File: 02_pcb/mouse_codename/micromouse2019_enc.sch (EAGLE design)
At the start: 0 parts

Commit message: schematic and pcb created
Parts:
- added C1: (no value), rcl:C-USC0402
- added IC1: AS5047D-ATSM, parts_not_managed:AS5047D-ATSM
- added R1, R2, R3: (no value), rcl:R-US_R0402
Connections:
- new net +3V3: C1.1, IC1.VDD, IC1.VDD3V, R1.2
- new net A: IC1.B
- new net B: IC1.A
- new net GND: C1.2, IC1.GND, IC1.TEST, R2.1, R3.1
- new net I: IC1.I/PWM
- new net N$1: IC1.CSN, R1.1
- new net N$2: IC1.CLK, R2.2
- new net N$3: IC1.MOSI, R3.2
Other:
- note added: "The LDO regulator is not intended to power any other loads, and it needs a 1 μF capacitor to ground located close to the chip"
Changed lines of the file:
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@@
 </classes>
 <parts>
+<part name="IC1" library="parts_not_managed" deviceset="AS5047D-ATSM" device=""/>
+<part name="R1" library="rcl" library_urn="urn:adsk.eagle:library:334" deviceset="R-US_" device="R0402" package3d_urn="urn:adsk.eagle:package:23547/3"/>
+<part name="R2" library="rcl" library_urn="urn:adsk.eagle:library:334" deviceset="R-US_" device="R0402" package3d_urn="urn:adsk.eagle:package:23547/3"/>
+<part name="R3" library="rcl" library_urn="urn:adsk.eagle:library:334" deviceset="R-US_" device="R0402" package3d_urn="urn:adsk.eagle:package:23547/3"/>
+<part name="+3V1" library="supply1" library_urn="urn:adsk.eagle:library:371" deviceset="+3V3" device=""/>
+<part name="GND1" library="supply1" library_urn="urn:adsk.eagle:library:371" deviceset="GND" device=""/>
+<part name="GND2" library="supply1" library_urn="urn:adsk.eagle:library:371" deviceset="GND" device=""/>
+<part name="GND3" library="supply1" library_urn="urn:adsk.eagle:library:371" deviceset="GND" device=""/>
+<part name="GND4" library="supply1" library_urn="urn:adsk.eagle:library:371" deviceset="GND" device=""/>
+<part name="C1" library="rcl" library_urn="urn:adsk.eagle:library:334" deviceset="C-US" device="C0402" package3d_urn="urn:adsk.eagle:package:23626/2"/>
+<part name="GND5" library="supply1" library_urn="urn:adsk.eagle:library:371" deviceset="GND" device=""/>
+<part name="+3V2" library="supply1" library_urn="urn:adsk.eagle:library:371" deviceset="+3V3" device=""/>
+<part name="GND6" library="supply1" library_urn="urn:adsk.eagle:library:371" deviceset="GND" device=""/>
+<part name="+3V3" library="supply1" library_urn="urn:adsk.eagle:library:371" deviceset="+3V3" device=""/>
 </parts>
 <sheets>
 <sheet>
 <plain>
+<text x="139.7" y="15.24" size="1.778" layer="97"> The LDO regulator is not intended to power any other
+loads, and it needs a 1 μF capacitor to ground located close to
+the chip</text>
 </plain>
 <instances>
+<instance part="IC1" gate="G$1" x="45.72" y="66.04" smashed="yes">
+<attribute name="NAME" x="72.39" y="73.66" size="1.778" layer="95" align="center-left"/>
+<attribute name="VALUE" x="72.39" y="71.12" size="1.778" layer="96" align="center-left"/>
+</instance>
+<instance part="R1" gate="G$1" x="40.64" y="73.66" smashed="yes" rot="R90">
+<attribute name="NAME" x="39.1414" y="69.85" size="1.778" layer="95" rot="R90"/>
+<attribute name="VALUE" x="43.942" y="69.85" size="1.778" layer="96" rot="R90"/>
+</instance>
+<instance part="R2" gate="G$1" x="17.78" y="50.8" smashed="yes" rot="R90">
+<attribute name="NAME" x="16.2814" y="46.99" size="1.778" layer="95" rot="R90"/>
+<attribute name="VALUE" x="21.082" y="46.99" size="1.778" layer="96" rot="R90"/>
+</instance>
+<instance part="R3" gate="G$1" x="25.4" y="50.8" smashed="yes" rot="R90">
+<attribute name="NAME" x="23.9014" y="46.99" size="1.778" layer="95" rot="R90"/>
+<attribute name="VALUE" x="28.702" y="46.99" size="1.778" layer="96" rot="R90"/>
+</instance>
+<instance part="+3V1" gate="G$1" x="40.64" y="86.36" smashed="yes">
+<attribute name="VALUE" x="38.862" y="81.788" size="1.778" layer="96" rot="R90"/>
+</instance>
+<instance part="GND1" gate="1" x="17.78" y="40.64" smashed="yes">
+<attribute name="VALUE" x="15.24" y="38.1" size="1.778" layer="96"/>
+</instance>
+<instance part="GND2" gate="1" x="25.4" y="40.64" smashed="yes">
+<attribute name="VALUE" x="22.86" y="38.1" size="1.778" layer="96"/>
+</instance>
+<instance part="GND3" gate="1" x="106.68" y="40.64" smashed="yes">
+<attribute name="VALUE" x="104.14" y="38.1" size="1.778" layer="96"/>
+</instance>
+<instance part="GND4" gate="1" x="33.02" y="40.64" smashed="yes">
+<attribute name="VALUE" x="30.48" y="38.1" size="1.778" layer="96"/>
+</instance>
+<instance part="C1" gate="G$1" x="88.9" y="50.8" smashed="yes">
+<attribute name="NAME" x="89.916" y="51.435" size="1.778" layer="95"/>
+<attribute name="VALUE" x="89.916" y="46.609" size="1.778" layer="96"/>
+</instance>
+<instance part="GND5" gate="1" x="88.9" y="40.64" smashed="yes">
+<attribute name="VALUE" x="86.36" y="38.1" size="1.778" layer="96"/>
+</instance>
+<instance part="+3V2" gate="G$1" x="99.06" y="60.96" smashed="yes">
+<attribute name="VALUE" x="97.536" y="55.88" size="1.778" layer="96" rot="R90"/>
+</instance>
+<instance part="GND6" gate="1" x="129.54" y="40.64" smashed="yes">
+<attribute name="VALUE" x="127" y="38.1" size="1.778" layer="96"/>
+</instance>
+<instance part="+3V3" gate="G$1" x="129.54" y="71.12" smashed="yes">
+<attribute name="VALUE" x="128.016" y="66.04" size="1.778" layer="96" rot="R90"/>
+</instance>
 </instances>
 <busses>
 </busses>
 <nets>
+<net name="N$1" class="0">
+<segment>
+<pinref part="IC1" gate="G$1" pin="CSN"/>
+<pinref part="R1" gate="G$1" pin="1"/>
+<wire x1="45.72" y1="66.04" x2="40.64" y2="66.04" width="0.1524" layer="91"/>
+<wire x1="40.64" y1="66.04" x2="40.64" y2="68.58" width="0.1524" layer="91"/>
+</segment>
+</net>
+<net name="+3V3" class="0">
+<segment>
+<pinref part="R1" gate="G$1" pin="2"/>
+<pinref part="+3V1" gate="G$1" pin="+3V3"/>
+<wire x1="40.64" y1="78.74" x2="40.64" y2="83.82" width="0.1524" layer="91"/>
+</segment>
+<segment>
+<wire x1="99.06" y1="58.42" x2="99.06" y2="55.88" width="0.1524" layer="91"/>
+<pinref part="IC1" gate="G$1" pin="VDD3V"/>
+<wire x1="76.2" y1="60.96" x2="78.74" y2="60.96" width="0.1524" layer="91"/>
+<wire x1="78.74" y1="60.96" x2="78.74" y2="58.42" width="0.1524" layer="91"/>
+<pinref part="IC1" gate="G$1" pin="VDD"/>
+<wire x1="76.2" y1="58.42" x2="78.74" y2="58.42" width="0.1524" layer="91"/>
+<pinref part="C1" gate="G$1" pin="1"/>
+<wire x1="88.9" y1="53.34" x2="88.9" y2="55.88" width="0.1524" layer="91"/>
+<wire x1="88.9" y1="55.88" x2="88.9" y2="58.42" width="0.1524" layer="91"/>
+<wire x1="88.9" y1="58.42" x2="78.74" y2="58.42" width="0.1524" layer="91"/>
+<junction x="78.74" y="58.42"/>
+<wire x1="99.06" y1="55.88" x2="88.9" y2="55.88" width="0.1524" layer="91"/>
+<junction x="88.9" y="55.88"/>
+<pinref part="+3V2" gate="G$1" pin="+3V3"/>
+</segment>
+<segment>
+<pinref part="+3V3" gate="G$1" pin="+3V3"/>
+<wire x1="134.62" y1="60.96" x2="129.54" y2="60.96" width="0.1524" layer="91"/>
+<wire x1="129.54" y1="60.96" x2="129.54" y2="68.58" width="0.1524" layer="91"/>
+</segment>
+</net>
+<net name="N$2" class="0">
+<segment>
+<pinref part="IC1" gate="G$1" pin="CLK"/>
+<pinref part="R2" gate="G$1" pin="2"/>
+<wire x1="45.72" y1="63.5" x2="17.78" y2="63.5" width="0.1524" layer="91"/>
+<wire x1="17.78" y1="63.5" x2="17.78" y2="55.88" width="0.1524" layer="91"/>
+</segment>
+</net>
+<net name="N$3" class="0">
+<segment>
+<pinref part="IC1" gate="G$1" pin="MOSI"/>
+<pinref part="R3" gate="G$1" pin="2"/>
+<wire x1="45.72" y1="58.42" x2="25.4" y2="58.42" width="0.1524" layer="91"/>
+<wire x1="25.4" y1="58.42" x2="25.4" y2="55.88" width="0.1524" layer="91"/>
+</segment>
+</net>
+<net name="GND" class="0">
+<segment>
+<pinref part="R2" gate="G$1" pin="1"/>
+<pinref part="GND1" gate="1" pin="GND"/>
+<wire x1="17.78" y1="45.72" x2="17.78" y2="43.18" width="0.1524" layer="91"/>
+</segment>
+<segment>
+<pinref part="R3" gate="G$1" pin="1"/>
+<pinref part="GND2" gate="1" pin="GND"/>
+<wire x1="25.4" y1="45.72" x2="25.4" y2="43.18" width="0.1524" layer="91"/>
+</segment>
+<segment>
+<pinref part="IC1" gate="G$1" pin="GND"/>
+<wire x1="76.2" y1="63.5" x2="106.68" y2="63.5" width="0.1524" layer="91"/>
+<pinref part="GND3" gate="1" pin="GND"/>
+<wire x1="106.68" y1="63.5" x2="106.68" y2="43.18" width="0.1524" layer="91"/>
+</segment>
+<segment>
+<pinref part="IC1" gate="G$1" pin="TEST"/>
+<pinref part="GND4" gate="1" pin="GND"/>
+<wire x1="45.72" y1="55.88" x2="33.02" y2="55.88" width="0.1524" layer="91"/>
+<wire x1="33.02" y1="55.88" x2="33.02" y2="43.18" width="0.1524" layer="91"/>
+</segment>
+<segment>
+<pinref part="C1" gate="G$1" pin="2"/>
+<pinref part="GND5" gate="1" pin="GND"/>
+<wire x1="88.9" y1="45.72" x2="88.9" y2="43.18" width="0.1524" layer="91"/>
+</segment>
+<segment>
+<wire x1="134.62" y1="50.8" x2="129.54" y2="50.8" width="0.1524" layer="91"/>
+<pinref part="GND6" gate="1" pin="GND"/>
+<wire x1="129.54" y1="50.8" x2="129.54" y2="43.18" width="0.1524" layer="91"/>
+</segment>
+</net>
+<net name="A" class="0">
+<segment>
+<pinref part="IC1" gate="G$1" pin="B"/>
+<wire x1="45.72" y1="53.34" x2="40.64" y2="53.34" width="0.1524" layer="91"/>
+<label x="40.64" y="53.34" size="1.778" layer="95"/>
+</segment>
+<segment>
+<wire x1="134.62" y1="58.42" x2="124.46" y2="58.42" width="0.1524" layer="91"/>
+<label x="124.46" y="58.42" size="1.778" layer="95"/>
+</segment>
+</net>
+<net name="B" class="0">
+<segment>
+<pinref part="IC1" gate="G$1" pin="A"/>
+<wire x1="45.72" y1="50.8" x2="40.64" y2="50.8" width="0.1524" layer="91"/>
+<label x="40.64" y="50.8" size="1.778" layer="95"/>
+</segment>
+<segment>
+<wire x1="134.62" y1="55.88" x2="124.46" y2="55.88" width="0.1524" layer="91"/>
+<label x="124.46" y="55.88" size="1.778" layer="95"/>
+</segment>
+</net>
+<net name="I" class="0">
+<segment>
+<pinref part="IC1" gate="G$1" pin="I/PWM"/>
+<wire x1="76.2" y1="66.04" x2="81.28" y2="66.04" width="0.1524" layer="91"/>
+<label x="78.74" y="66.04" size="1.778" layer="95"/>
+</segment>
+<segment>
+<wire x1="134.62" y1="53.34" x2="124.46" y2="53.34" width="0.1524" layer="91"/>
+<label x="124.46" y="53.34" size="1.778" layer="95"/>
+</segment>
+</net>
 </nets>
 </sheet>
@@
 </drawing>
 <compatibility>
+<note version="6.3" minversion="6.2.2" severity="warning">
+Since Version 6.2.2 text objects can contain more than one line,
+which will not be processed correctly with this version.
+</note>
 <note version="8.2" severity="warning">
 Since Version 8.2, EAGLE supports online libraries. The ids

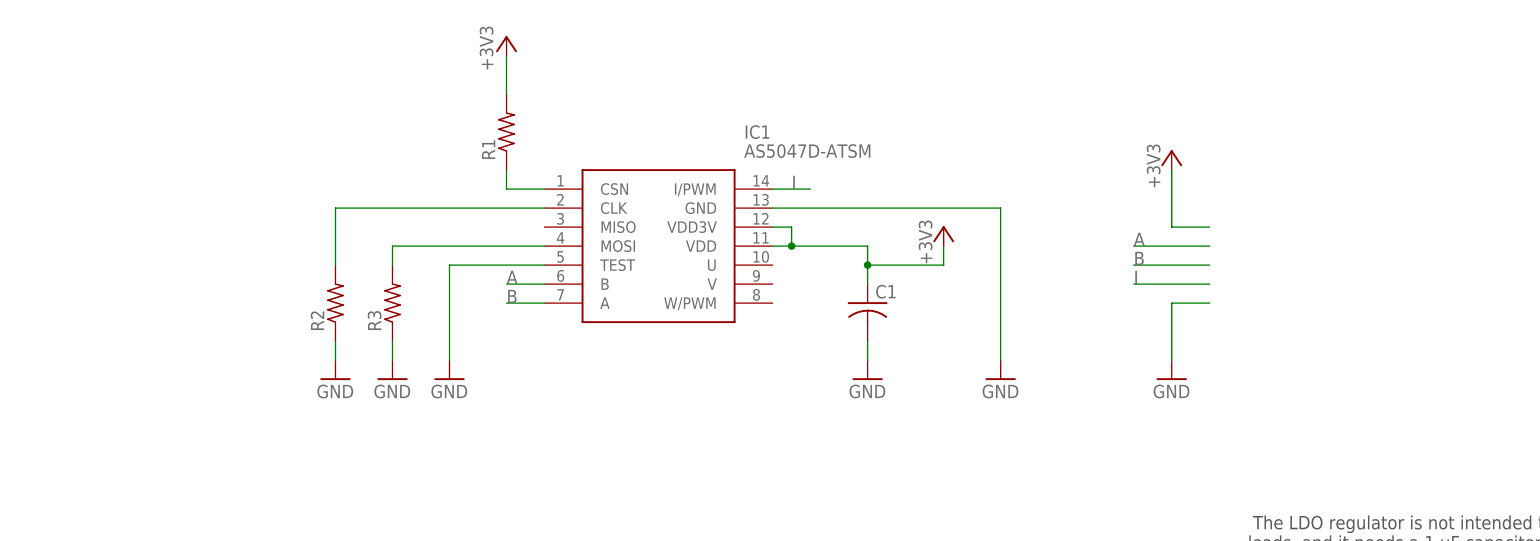
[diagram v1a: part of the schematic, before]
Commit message: Updated enc pcb, spi connector added
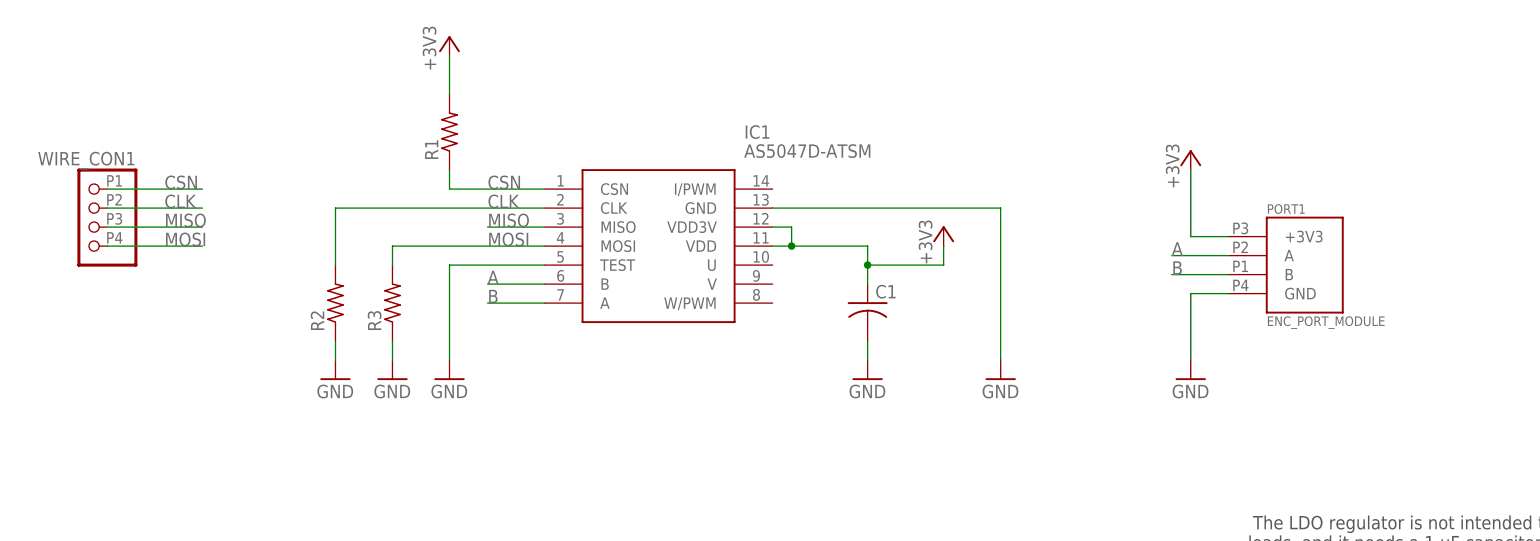
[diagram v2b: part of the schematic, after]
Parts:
- added PORT1: ENC_PORT_MODULE, parts_not_managed:ENC_PORT_MODULE
- added WIRE_CON1: CON_WIRE, parts_not_managed:CON_WIRE
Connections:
- removed net I: IC1.I/PWM
- removed net N$1: IC1.CSN, R1.1
- removed net N$2: IC1.CLK, R2.2
- removed net N$3: IC1.MOSI, R3.2
- new net CLK: IC1.CLK, R2.2, WIRE_CON1.2
- new net CSN: IC1.CSN, R1.1, WIRE_CON1.1
- new net MISO: IC1.MISO, WIRE_CON1.3
- new net MOSI: IC1.MOSI, R3.2, WIRE_CON1.4
- net +3V3: now also PORT1.+3V3
- net A: now also PORT1.A
- net B: now also PORT1.B
- net GND: now also PORT1.GND
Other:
- moved on the sheet: R1

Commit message: Names and values on PCB arranged, values for R and C elements added
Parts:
- C1: value (none) -> 100n
- IC1: value AS5047D-ATSM -> AS5047D
- R1, R2, R3: value (none) -> 10k
- renumbered WIRE_CON1 to SPI
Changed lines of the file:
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@@
 </classes>
 <parts>
-<part name="IC1" library="parts_not_managed" deviceset="AS5047D-ATSM" device=""/>
-<part name="R1" library="rcl" library_urn="urn:adsk.eagle:library:334" deviceset="R-US_" device="R0402" package3d_urn="urn:adsk.eagle:package:23547/3"/>
-<part name="R2" library="rcl" library_urn="urn:adsk.eagle:library:334" deviceset="R-US_" device="R0402" package3d_urn="urn:adsk.eagle:package:23547/3"/>
-<part name="R3" library="rcl" library_urn="urn:adsk.eagle:library:334" deviceset="R-US_" device="R0402" package3d_urn="urn:adsk.eagle:package:23547/3"/>
+<part name="IC1" library="parts_not_managed" deviceset="AS5047D-ATSM" device="" value="AS5047D"/>
+<part name="R1" library="rcl" library_urn="urn:adsk.eagle:library:334" deviceset="R-US_" device="R0402" package3d_urn="urn:adsk.eagle:package:23547/3" value="10k"/>
+<part name="R2" library="rcl" library_urn="urn:adsk.eagle:library:334" deviceset="R-US_" device="R0402" package3d_urn="urn:adsk.eagle:package:23547/3" value="10k"/>
+<part name="R3" library="rcl" library_urn="urn:adsk.eagle:library:334" deviceset="R-US_" device="R0402" package3d_urn="urn:adsk.eagle:package:23547/3" value="10k"/>
 <part name="+3V1" library="supply1" library_urn="urn:adsk.eagle:library:371" deviceset="+3V3" device=""/>
 <part name="GND1" library="supply1" library_urn="urn:adsk.eagle:library:371" deviceset="GND" device=""/>
@@
 <part name="GND3" library="supply1" library_urn="urn:adsk.eagle:library:371" deviceset="GND" device=""/>
 <part name="GND4" library="supply1" library_urn="urn:adsk.eagle:library:371" deviceset="GND" device=""/>
-<part name="C1" library="rcl" library_urn="urn:adsk.eagle:library:334" deviceset="C-US" device="C0402" package3d_urn="urn:adsk.eagle:package:23626/2"/>
+<part name="C1" library="rcl" library_urn="urn:adsk.eagle:library:334" deviceset="C-US" device="C0402" package3d_urn="urn:adsk.eagle:package:23626/2" value="100n"/>
 <part name="GND5" library="supply1" library_urn="urn:adsk.eagle:library:371" deviceset="GND" device=""/>
 <part name="+3V2" library="supply1" library_urn="urn:adsk.eagle:library:371" deviceset="+3V3" device=""/>
@@
 <part name="+3V3" library="supply1" library_urn="urn:adsk.eagle:library:371" deviceset="+3V3" device=""/>
 <part name="PORT1" library="parts_not_managed" deviceset="ENC_PORT" device="_MODULE"/>
-<part name="WIRE_CON1" library="parts_not_managed" deviceset="CON_WIRE" device=""/>
+<part name="SPI" library="parts_not_managed" deviceset="CON_WIRE" device=""/>
 </parts>
 <sheets>
@@
 <attribute name="VALUE" x="142.24" y="47.752" size="1.27" layer="95"/>
 </instance>
-<instance part="WIRE_CON1" gate="G$1" x="-15.24" y="60.96" smashed="yes" rot="MR0">
+<instance part="SPI" gate="G$1" x="-15.24" y="60.96" smashed="yes" rot="MR0">
 <attribute name="NAME" x="-8.89" y="69.215" size="1.778" layer="95" rot="MR0"/>
 </instance>
@@
 <wire x1="-12.7" y1="63.5" x2="0" y2="63.5" width="0.1524" layer="91"/>
 <label x="-5.08" y="63.5" size="1.778" layer="95"/>
-<pinref part="WIRE_CON1" gate="G$1" pin="2"/>
+<pinref part="SPI" gate="G$1" pin="2"/>
 </segment>
 </net>
@@
 <wire x1="-12.7" y1="66.04" x2="0" y2="66.04" width="0.1524" layer="91"/>
 <label x="-5.08" y="66.04" size="1.778" layer="95"/>
-<pinref part="WIRE_CON1" gate="G$1" pin="1"/>
+<pinref part="SPI" gate="G$1" pin="1"/>
 </segment>
 <segment>
@@
 <wire x1="-12.7" y1="60.96" x2="0" y2="60.96" width="0.1524" layer="91"/>
 <label x="-5.08" y="60.96" size="1.778" layer="95"/>
-<pinref part="WIRE_CON1" gate="G$1" pin="3"/>
+<pinref part="SPI" gate="G$1" pin="3"/>
 </segment>
 <segment>
@@
 <wire x1="-12.7" y1="58.42" x2="0" y2="58.42" width="0.1524" layer="91"/>
 <label x="-5.08" y="58.42" size="1.778" layer="95"/>
-<pinref part="WIRE_CON1" gate="G$1" pin="4"/>
-</segment>
-<segment>
+<pinref part="SPI" gate="G$1" pin="4"/>
+</segment>
+<segment>

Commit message: encoder pcb updated
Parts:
- IC1: device parts_not_managed:AS5047D-ATSM -> parts:AS5047D-ATSM
- PORT1: device parts_not_managed:ENC_PORT_MODULE -> parts:ENC_PORT_MODULE
- SPI: device parts_not_managed:CON_WIRE -> parts:CON_WIRE

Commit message: encoder board libs replaced with 0-micromouse.lbr
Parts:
- C1: device rcl:C-USC0402 -> 0-micromouse2019:C-USC0402
- IC1: device parts:AS5047D-ATSM -> 0-micromouse2019:AS5047D-ATSM
- PORT1: device parts:ENC_PORT_MODULE -> 0-micromouse2019:ENC_PORT_MODULE
- R1, R2, R3: device rcl:R-US_R0402 -> 0-micromouse2019:R-US_R0402
- SPI: device parts:CON_WIRE -> 0-micromouse2019:CON_WIRE
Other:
- moved on the sheet: C1, IC1, PORT1, R1, R2, R3, SPI

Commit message: Connectors replaced: IRDx4 & IRDVCC & SPI
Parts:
- removed SPI: CON_WIRE, 0-micromouse2019:CON_WIRE
- added U$1: CONN_SPI, 0-micromouse2019:CONN_SPI
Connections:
- net CLK: now also U$1.P3; no longer SPI.2
- net CSN: now also U$1.P4; no longer SPI.1
- net MISO: now also U$1.P2; no longer SPI.3
- net MOSI: now also U$1.P1; no longer SPI.4
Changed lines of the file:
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@@
 <part name="GND6" library="0-micromouse2019" deviceset="GND" device=""/>
 <part name="+3V3" library="0-micromouse2019" deviceset="+3V3" device=""/>
-<part name="SPI" library="0-micromouse2019" deviceset="CON_WIRE" device=""/>
 <part name="PORT1" library="0-micromouse2019" deviceset="ENC_PORT" device="_MODULE"/>
 <part name="FRAME1" library="frames" library_urn="urn:adsk.eagle:library:229" deviceset="DINA4_L" device=""/>
+<part name="U$1" library="0-micromouse2019" deviceset="CONN_SPI" device="" package3d_urn="urn:adsk.eagle:package:9165666/2"/>
 </parts>
 <sheets>
@@
 <attribute name="VALUE" x="173.736" y="109.22" size="1.778" layer="96" rot="R90"/>
 </instance>
-<instance part="SPI" gate="G$1" x="27.94" y="104.14" smashed="yes" rot="MR0">
-<attribute name="NAME" x="34.29" y="112.395" size="1.778" layer="95" rot="MR0"/>
-</instance>
 <instance part="PORT1" gate="G$1" x="185.166" y="92.71" smashed="yes">
 <attribute name="NAME" x="185.674" y="106.426" size="1.27" layer="95"/>
@@
 <attribute name="SHEET" x="248.92" y="1.27" size="2.54" layer="94"/>
 <attribute name="DRAWING_NAME" x="180.34" y="19.05" size="2.54" layer="94"/>
+</instance>
+<instance part="U$1" gate="G$1" x="22.86" y="101.6" smashed="yes" rot="R90">
+<attribute name="NAME" x="20.066" y="111.76" size="1.27" layer="95"/>
+<attribute name="VALUE" x="20.32" y="96.52" size="1.27" layer="96"/>
 </instance>
 </instances>
@@
 <wire x1="30.48" y1="106.68" x2="43.18" y2="106.68" width="0.1524" layer="91"/>
 <label x="38.1" y="106.68" size="1.778" layer="95"/>
-<pinref part="SPI" gate="G$1" pin="2"/>
+<pinref part="U$1" gate="G$1" pin="P3"/>
 </segment>
 </net>
@@
 <wire x1="30.48" y1="109.22" x2="43.18" y2="109.22" width="0.1524" layer="91"/>
 <label x="38.1" y="109.22" size="1.778" layer="95"/>
-<pinref part="SPI" gate="G$1" pin="1"/>
+<pinref part="U$1" gate="G$1" pin="P4"/>
 </segment>
 <segment>
@@
 <wire x1="30.48" y1="104.14" x2="43.18" y2="104.14" width="0.1524" layer="91"/>
 <label x="38.1" y="104.14" size="1.778" layer="95"/>
-<pinref part="SPI" gate="G$1" pin="3"/>
+<pinref part="U$1" gate="G$1" pin="P2"/>
 </segment>
 <segment>
@@
 <wire x1="30.48" y1="101.6" x2="43.18" y2="101.6" width="0.1524" layer="91"/>
 <label x="38.1" y="101.6" size="1.778" layer="95"/>
-<pinref part="SPI" gate="G$1" pin="4"/>
-</segment>
-<segment>
+<pinref part="U$1" gate="G$1" pin="P1"/>
+</segment>
+<segment>
